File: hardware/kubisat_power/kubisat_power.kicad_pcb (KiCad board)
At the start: 2 copper layers, 80 x 80 mm, 82 parts, among them J1 USB_C_Receptacle_PowerOnly_6P, J2 B2B-PH-SM4-TB_LF__SN_, J3 Conn_01x06_MountingPin, Q1 Si2305, U2 INA3221, U3 LN2220, U4 CN3791, U5 TP4056, U6 DW01A, U7 FS8205

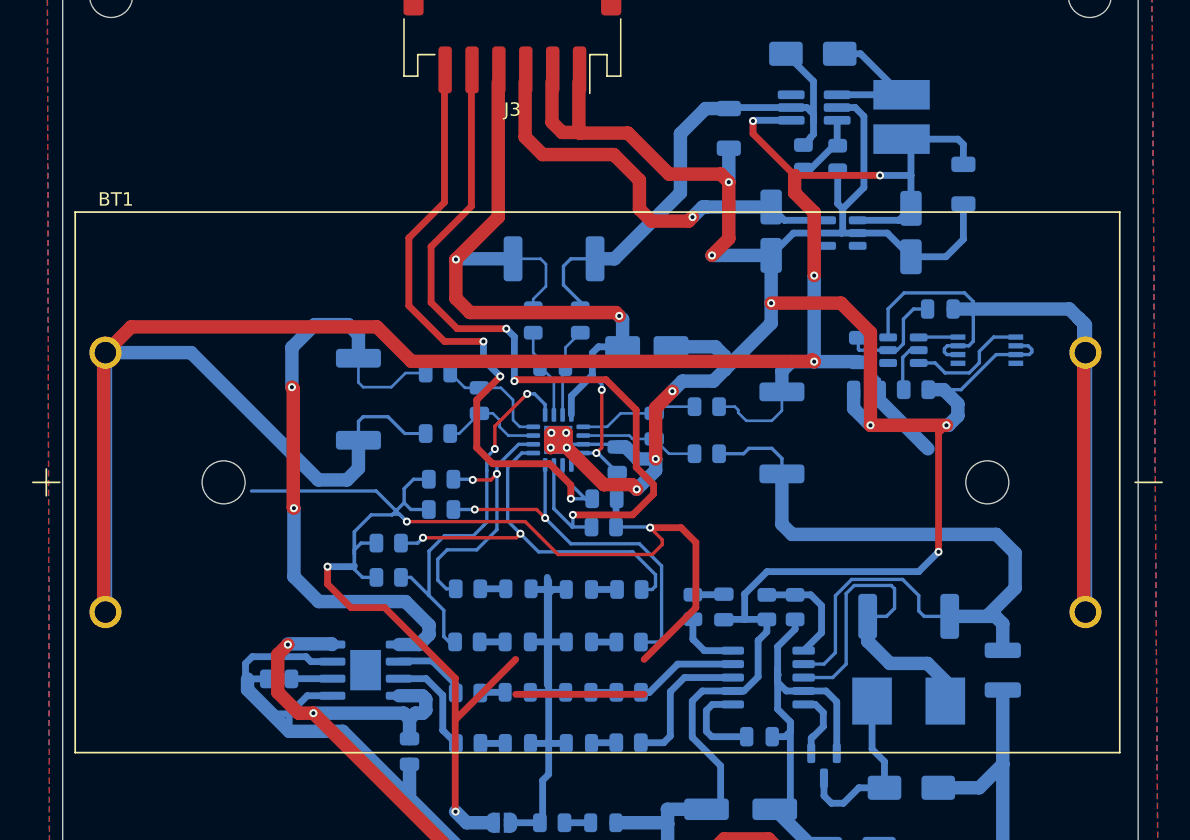
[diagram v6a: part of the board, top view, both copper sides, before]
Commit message: added software - ina3221 and camera scripts
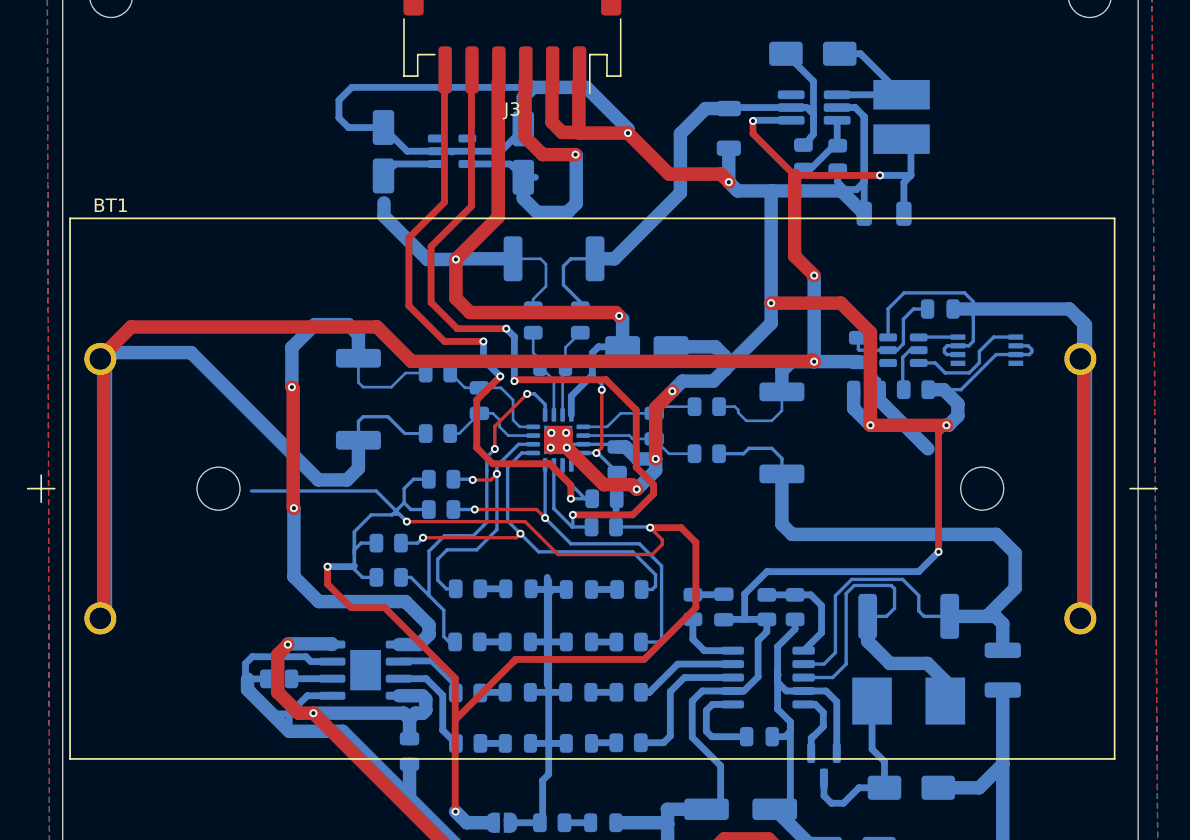
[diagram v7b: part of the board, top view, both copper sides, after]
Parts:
- R12: value 10k -> 100k
- moved C2 39.7 mm to (38.8, 35.2), turned to 90 degrees
- moved U1 29.7 mm to (43.9, 35.1), turned to 0 degrees
- moved C8 19.3 mm to (49.2, 35.3), turned to 90 degrees
- moved C9 6.30 mm to (76.0, 39.8), turned to 180 degrees
- moved BT1 0.60 mm to (54.4, 60.2)
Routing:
- net GND: track 439.0 -> 473.5 mm
- net 5V_SENSE_OUT: track 181.0 -> 189.0 mm
- net +3V3: track 31.3 -> 23.7 mm
- net SOLAR_SENSE_OUT: track 220.9 -> 215.3 mm
